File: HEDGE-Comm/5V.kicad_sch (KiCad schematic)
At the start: 11 parts, among them U2 MAX20402AFLA/VY+

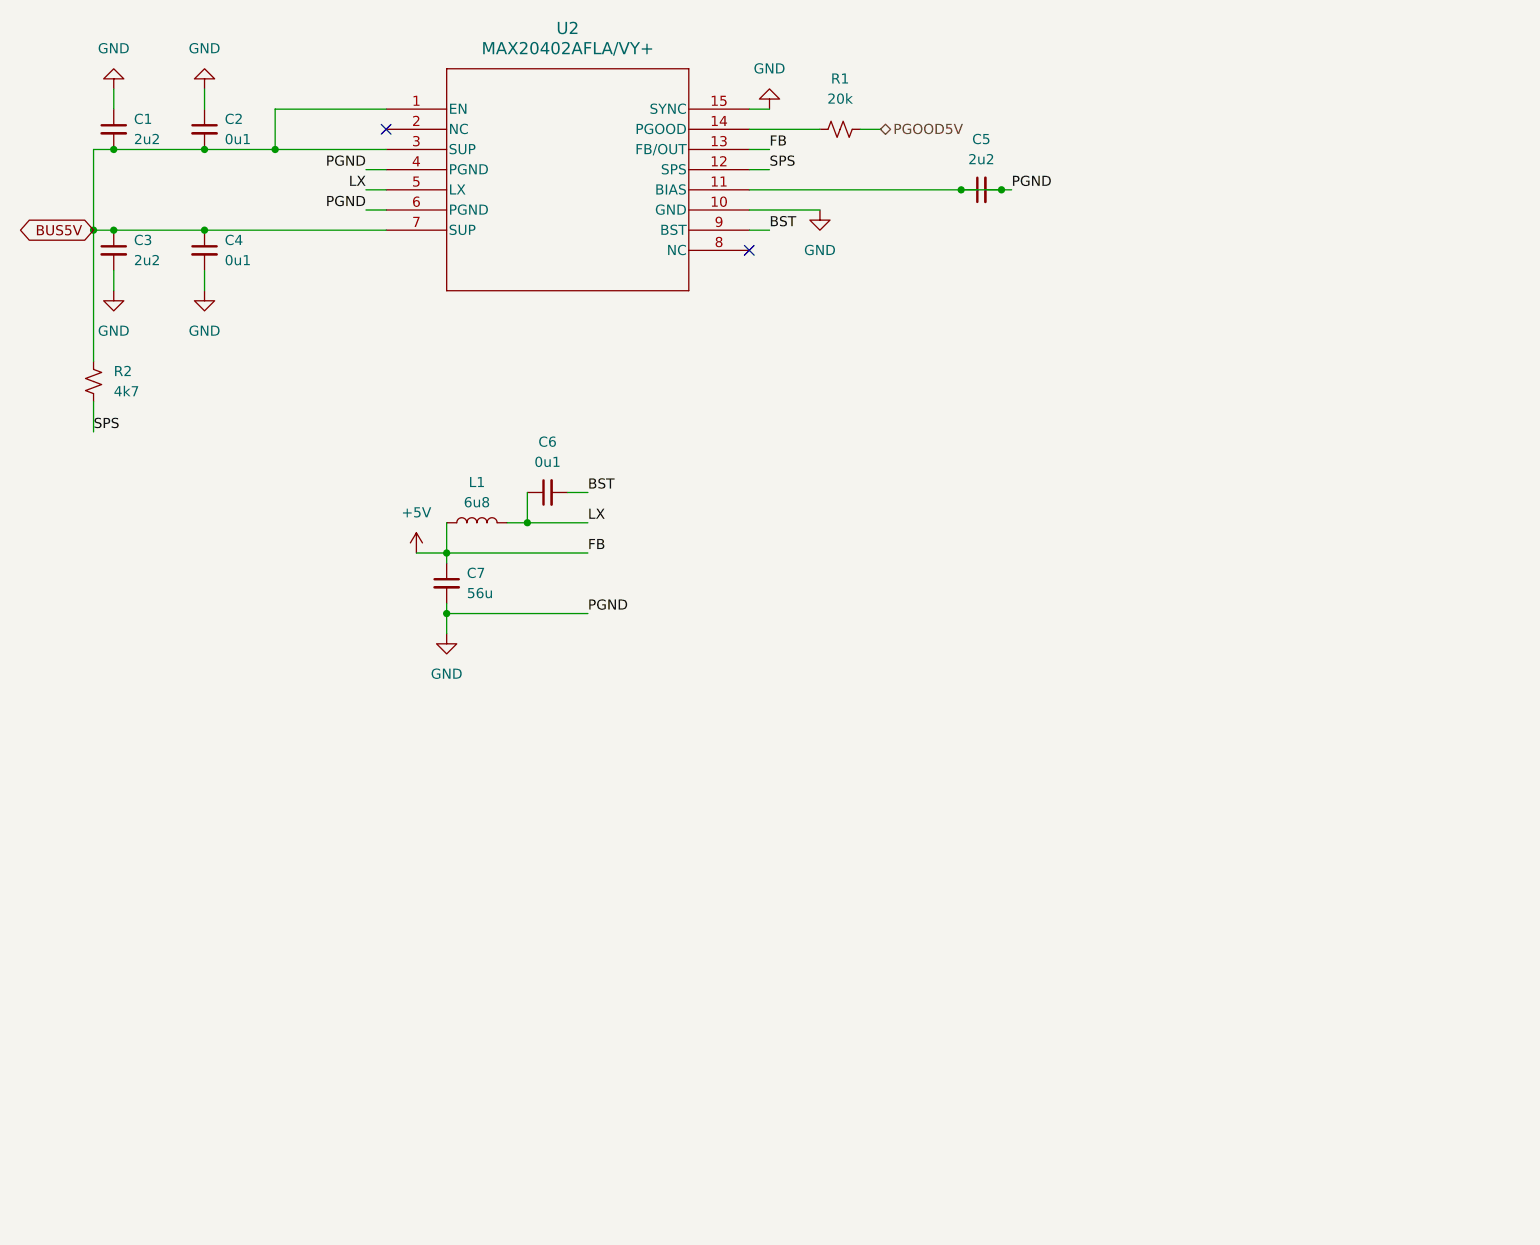
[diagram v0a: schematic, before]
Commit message: Refactor Data PCB files; enter RS485; enter Iridium radio power
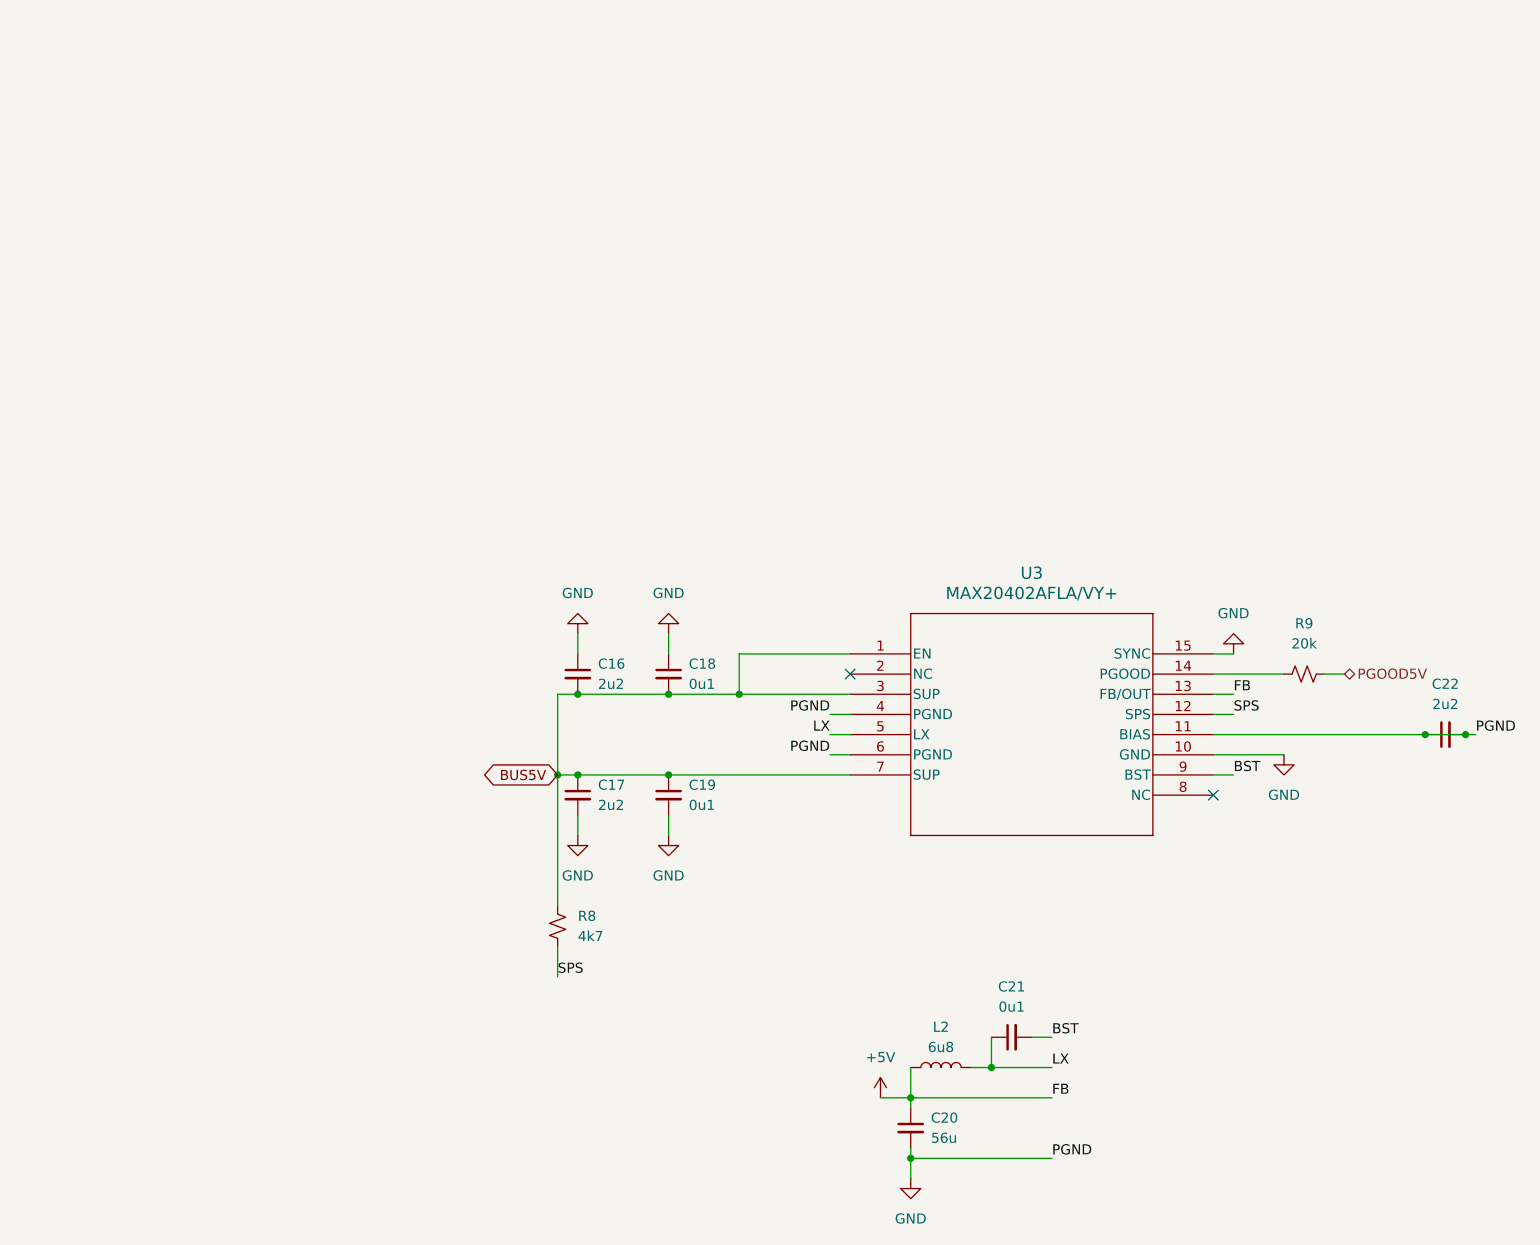
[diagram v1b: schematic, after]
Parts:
- removed C1, C3, C5: 2u2, symbol Device:C_Small
- removed C2, C4, C6: 0u1, symbol Device:C_Small
- removed C7: 56u, symbol Device:C_Small
- removed L1: 6u8, symbol Device:L
- removed R1: 20k, symbol Device:R_Small_US
- removed R2: 4k7, symbol Device:R_Small_US
- removed U2: MAX20402AFLA/VY+, 21-100532_90-100188_ADI, symbol MAX20402A:MAX20402AFLA_VY+
- added C16, C17, C22: 2u2, symbol Device:C_Small
- added C18, C19, C21: 0u1, symbol Device:C_Small
- added C20: 56u, symbol Device:C_Small
- added L2: 6u8, symbol Device:L
- added R8: 4k7, symbol Device:R_Small_US
- added R9: 20k, symbol Device:R_Small_US
- added U3: MAX20402AFLA/VY+, 21-100532_90-100188_ADI, symbol MAX20402A:MAX20402AFLA_VY+
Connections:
- net +5V: now also C20.1, L2.1, U3.13 (FB/OUT)
- net BST: now also C21.2, U3.9 (BST)
- net BUS5V: now also C16.2, C17.1, C18.2, C19.1, R8.2, U3.1 (EN), U3.3 (SUP), U3.7 (SUP)
- net GND: now also C16.1, C17.2, C18.1, C19.2, C20.2, C22.1, C22.2, U3.10 (GND), U3.11 (BIAS), U3.15 (SYNC), U3.4 (PGND), U3.6 (PGND)
- net LX: now also C21.1, L2.2, U3.5 (LX)
- net PGOOD5V: now also R9.2
- net SPS: now also R8.1, U3.12 (SPS)
- new net: R9.1, U3.14 (PGOOD)
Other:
- company: (none) -> Spacecraft Design Lab
- title: (none) -> HEDGE Comm PCB
